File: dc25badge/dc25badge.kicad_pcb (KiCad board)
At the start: 2 copper layers, 150.7 x 59.7 mm, 110 parts, among them P1 BATT, P2 USB_OTG, P3 CONN_CORTEX, SW1 RESET, SW2 PWR, SW3 MODE, SW4 BRIGHT, U1 MIC5305, U10 APA102, U11 APA102, U12 APA102, U13 APA102, U14 APA102, U15 APA102, U16 APA102, U17 APA102, U18 APA102, U19 APA102, U2 TPS61232, U20 APA102, U21 APA102, U22 APA102, U23 APA102, U24 APA102, U25 APA102, U26 APA102, U27 APA102, U28 APA102, U29 APA102, U3 ATSAMD21E18A-AU, U30 APA102, U31 APA102, U32 APA102, U33 APA102, U34 APA102, U35 APA102, U36 APA102, U37 APA102, U38 APA102, U39 APA102, U4 74AHCT125, U40 APA102, U41 APA102, U42 APA102, U43 APA102, U44 APA102, U45 APA102, U46 APA102, U47 APA102, U48 APA102, U49 APA102, U5 APA102, U50 APA102, U51 APA102, U52 APA102, U53 APA102, U54 APA102, U55 APA102, U56 APA102, U57 APA102, U58 APA102, U59 APA102, U6 APA102, U60 APA102, U61 APA102, U62 APA102, U63 APA102, U64 APA102, U7 APA102, U8 APA102, U9 APA102, Y1 32.768k

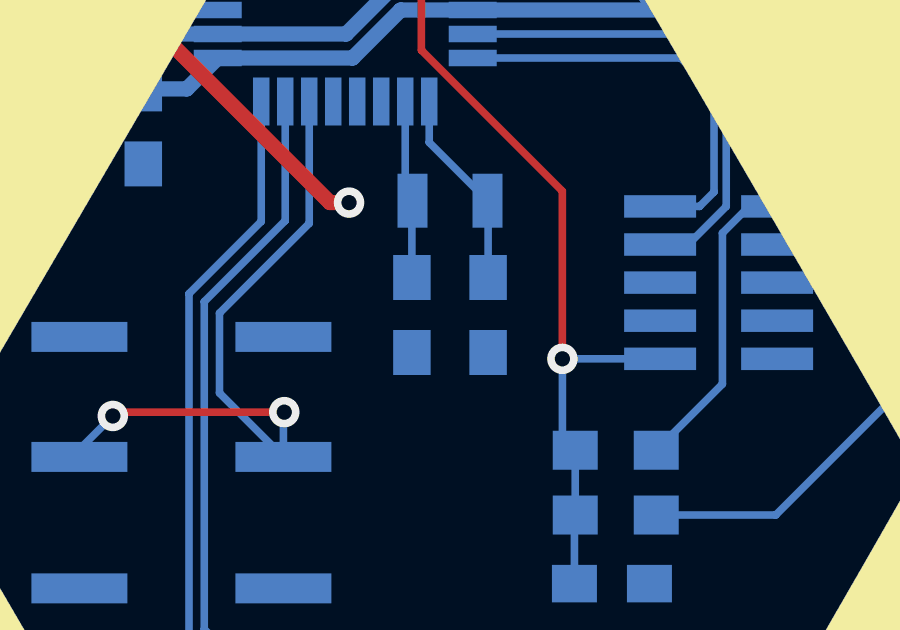
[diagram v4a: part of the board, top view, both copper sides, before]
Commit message: Switch to 0603 caps on oscillator.
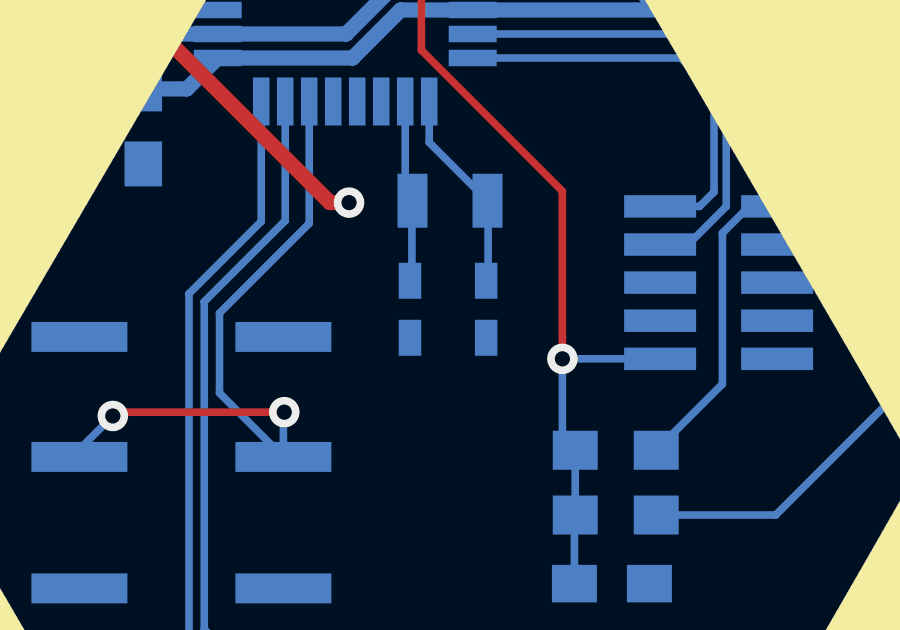
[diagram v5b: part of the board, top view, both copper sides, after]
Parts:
- C12, C13: footprint Capacitors_SMD:C_0805_HandSoldering -> Capacitors_SMD:C_0603_HandSoldering
- L1: value L_Core_Ferrite -> 1uH
- moved C12 0.20 mm to (76.3, 51.1)
- moved C13 0.20 mm to (78.9, 51.1)
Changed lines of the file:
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@@
   )
   (setup
-    (last_trace_width 1.016)
+    (last_trace_width 0.1524)
     (user_trace_width 0.1524)
     (user_trace_width 0.254)
@@
   )
   (module Capacitors_SMD:C_0805_HandSoldering (layer B.Cu)
-    (at 76.3905 51.2445 270)
-    (descr "Capacitor SMD 0805, hand soldering")
-    (tags "capacitor 0805")
-    (attr smd)
-    (fp_text reference C12 (at -1.778 1.397 270) (layer B.SilkS)
-      (effects (font (size 0.4 0.4) (thickness 0.1)) (justify mirror))
-    )
-    (fp_text value 22pF (at 0 -2.1 270) (layer B.Fab) hide
-      (effects (font (size 1 1) (thickness 0.15)) (justify mirror))
-    )
-    (fp_line (start -1 -0.625) (end -1 0.625) (layer B.Fab) (width 0.15))
-    (fp_line (start 1 -0.625) (end -1 -0.625) (layer B.Fab) (width 0.15))
-    (fp_line (start 1 0.625) (end 1 -0.625) (layer B.Fab) (width 0.15))
-    (fp_line (start -1 0.625) (end 1 0.625) (layer B.Fab) (width 0.15))
-    (fp_line (start -2.3 1) (end 2.3 1) (layer B.CrtYd) (width 0.05))
-    (fp_line (start -2.3 -1) (end 2.3 -1) (layer B.CrtYd) (width 0.05))
-    (fp_line (start -2.3 1) (end -2.3 -1) (layer B.CrtYd) (width 0.05))
-    (fp_line (start 2.3 1) (end 2.3 -1) (layer B.CrtYd) (width 0.05))
-    (fp_line (start 0.5 0.85) (end -0.5 0.85) (layer B.SilkS) (width 0.15))
-    (fp_line (start -0.5 -0.85) (end 0.5 -0.85) (layer B.SilkS) (width 0.15))
-    (pad 1 smd rect (at -1.25 0 270) (size 1.5 1.25) (layers B.Cu B.Paste B.Mask)
-      (net 7 XOUT32))
-    (pad 2 smd rect (at 1.25 0 270) (size 1.5 1.25) (layers B.Cu B.Paste B.Mask)
-      (net 1 GND))
-    (model Capacitors_SMD.3dshapes/C_0805_HandSoldering.wrl
-      (at (xyz 0 0 0))
-      (scale (xyz 1 1 1))
-      (rotate (xyz 0 0 0))
-    )
-  )
-  (module Capacitors_SMD:C_0805_HandSoldering (layer B.Cu)
-    (at 78.9305 51.2445 270)
-    (descr "Capacitor SMD 0805, hand soldering")
-    (tags "capacitor 0805")
-    (attr smd)
-    (fp_text reference C13 (at -1.651 -1.397 270) (layer B.SilkS)
-      (effects (font (size 0.4 0.4) (thickness 0.1)) (justify mirror))
-    )
-    (fp_text value 22pF (at 0 -2.1 270) (layer B.Fab) hide
-      (effects (font (size 1 1) (thickness 0.15)) (justify mirror))
-    )
-    (fp_line (start -1 -0.625) (end -1 0.625) (layer B.Fab) (width 0.15))
-    (fp_line (start 1 -0.625) (end -1 -0.625) (layer B.Fab) (width 0.15))
-    (fp_line (start 1 0.625) (end 1 -0.625) (layer B.Fab) (width 0.15))
-    (fp_line (start -1 0.625) (end 1 0.625) (layer B.Fab) (width 0.15))
-    (fp_line (start -2.3 1) (end 2.3 1) (layer B.CrtYd) (width 0.05))
-    (fp_line (start -2.3 -1) (end 2.3 -1) (layer B.CrtYd) (width 0.05))
-    (fp_line (start -2.3 1) (end -2.3 -1) (layer B.CrtYd) (width 0.05))
-    (fp_line (start 2.3 1) (end 2.3 -1) (layer B.CrtYd) (width 0.05))
-    (fp_line (start 0.5 0.85) (end -0.5 0.85) (layer B.SilkS) (width 0.15))
-    (fp_line (start -0.5 -0.85) (end 0.5 -0.85) (layer B.SilkS) (width 0.15))
-    (pad 1 smd rect (at -1.25 0 270) (size 1.5 1.25) (layers B.Cu B.Paste B.Mask)
-      (net 8 XIN32))
-    (pad 2 smd rect (at 1.25 0 270) (size 1.5 1.25) (layers B.Cu B.Paste B.Mask)
-      (net 1 GND))
-    (model Capacitors_SMD.3dshapes/C_0805_HandSoldering.wrl
-      (at (xyz 0 0 0))
-      (scale (xyz 1 1 1))
-      (rotate (xyz 0 0 0))
-    )
-  )
-  (module Capacitors_SMD:C_0805_HandSoldering (layer B.Cu)
     (at 101.219 67.818 270)
     (descr "Capacitor SMD 0805, hand soldering")
@@
       (effects (font (size 0.5 0.5) (thickness 0.1)) (justify mirror))
     )
-    (fp_text value L_Core_Ferrite (at 0 -3.4 180) (layer B.Fab) hide
+    (fp_text value 1uH (at 0 -3.4 180) (layer B.Fab) hide
       (effects (font (size 1 1) (thickness 0.15)) (justify mirror))
     )
@@
     )
   )
+  (module Capacitors_SMD:C_0603_HandSoldering (layer B.Cu)
+    (at 76.327 51.054 270)
+    (descr "Capacitor SMD 0603, hand soldering")
+    (tags "capacitor 0603")
+    (attr smd)
+    (fp_text reference C12 (at -1.27 1.143 270) (layer B.SilkS)
+      (effects (font (size 0.4 0.4) (thickness 0.1)) (justify mirror))
+    )
+    (fp_text value 22pF (at 0 -1.9 270) (layer B.Fab) hide
+      (effects (font (size 1 1) (thickness 0.15)) (justify mirror))
+    )
+    (fp_line (start -0.8 -0.4) (end -0.8 0.4) (layer B.Fab) (width 0.15))
+    (fp_line (start 0.8 -0.4) (end -0.8 -0.4) (layer B.Fab) (width 0.15))
+    (fp_line (start 0.8 0.4) (end 0.8 -0.4) (layer B.Fab) (width 0.15))
+    (fp_line (start -0.8 0.4) (end 0.8 0.4) (layer B.Fab) (width 0.15))
+    (fp_line (start -1.85 0.75) (end 1.85 0.75) (layer B.CrtYd) (width 0.05))
+    (fp_line (start -1.85 -0.75) (end 1.85 -0.75) (layer B.CrtYd) (width 0.05))
+    (fp_line (start -1.85 0.75) (end -1.85 -0.75) (layer B.CrtYd) (width 0.05))
+    (fp_line (start 1.85 0.75) (end 1.85 -0.75) (layer B.CrtYd) (width 0.05))
+    (fp_line (start -0.35 0.6) (end 0.35 0.6) (layer B.SilkS) (width 0.15))
+    (fp_line (start 0.35 -0.6) (end -0.35 -0.6) (layer B.SilkS) (width 0.15))
+    (pad 1 smd rect (at -0.95 0 270) (size 1.2 0.75) (layers B.Cu B.Paste B.Mask)
+      (net 7 XOUT32))
+    (pad 2 smd rect (at 0.95 0 270) (size 1.2 0.75) (layers B.Cu B.Paste B.Mask)
+      (net 1 GND))
+    (model Capacitors_SMD.3dshapes/C_0603_HandSoldering.wrl
+      (at (xyz 0 0 0))
+      (scale (xyz 1 1 1))
+      (rotate (xyz 0 0 0))
+    )
+  )
+  (module Capacitors_SMD:C_0603_HandSoldering (layer B.Cu)
+    (at 78.867 51.054 270)
+    (descr "Capacitor SMD 0603, hand soldering")
+    (tags "capacitor 0603")
+    (attr smd)
+    (fp_text reference C13 (at -1.27 -1.143 270) (layer B.SilkS)
+      (effects (font (size 0.4 0.4) (thickness 0.1)) (justify mirror))
+    )
+    (fp_text value 22pF (at 0 -1.9 270) (layer B.Fab) hide
+      (effects (font (size 1 1) (thickness 0.15)) (justify mirror))
+    )
+    (fp_line (start -0.8 -0.4) (end -0.8 0.4) (layer B.Fab) (width 0.15))
+    (fp_line (start 0.8 -0.4) (end -0.8 -0.4) (layer B.Fab) (width 0.15))
+    (fp_line (start 0.8 0.4) (end 0.8 -0.4) (layer B.Fab) (width 0.15))
+    (fp_line (start -0.8 0.4) (end 0.8 0.4) (layer B.Fab) (width 0.15))
+    (fp_line (start -1.85 0.75) (end 1.85 0.75) (layer B.CrtYd) (width 0.05))
+    (fp_line (start -1.85 -0.75) (end 1.85 -0.75) (layer B.CrtYd) (width 0.05))
+    (fp_line (start -1.85 0.75) (end -1.85 -0.75) (layer B.CrtYd) (width 0.05))
+    (fp_line (start 1.85 0.75) (end 1.85 -0.75) (layer B.CrtYd) (width 0.05))
+    (fp_line (start -0.35 0.6) (end 0.35 0.6) (layer B.SilkS) (width 0.15))
+    (fp_line (start 0.35 -0.6) (end -0.35 -0.6) (layer B.SilkS) (width 0.15))
+    (pad 1 smd rect (at -0.95 0 270) (size 1.2 0.75) (layers B.Cu B.Paste B.Mask)
+      (net 8 XIN32))
+    (pad 2 smd rect (at 0.95 0 270) (size 1.2 0.75) (layers B.Cu B.Paste B.Mask)
+      (net 1 GND))
+    (model Capacitors_SMD.3dshapes/C_0603_HandSoldering.wrl
+      (at (xyz 0 0 0))
+      (scale (xyz 1 1 1))
+      (rotate (xyz 0 0 0))
+    )
+  )
   (gr_line (start 26.67 86.868) (end 44.323 56.515) (angle 90) (layer Edge.Cuts) (width 0.15))
   (gr_line (start 158.496 86.868) (end 26.67 86.868) (angle 90) (layer Edge.Cuts) (width 0.15))
@@
   (gr_line (start 44.323 56.515) (end 27.305 27.178) (angle 90) (layer Edge.Cuts) (width 0.15))
   (via (at 143.891 49.276) (size 1.016) (drill 0.508) (layers F.Cu B.Cu) (net 0))
-  (segment (start 123.079 43.453) (end 121.558 43.453) (width 1.016) (layer B.Cu) (net 1) (status 400000))
-  (segment (start 124.333 35.433) (end 124.333 33.909) (width 1.016) (layer B.Cu) (net 1) (status 800000))
+  (segment (start 123.079 43.453) (end 121.558 43.453) (width 1.016) (layer B.Cu) (net 1))
+  (segment (start 124.333 35.433) (end 124.333 33.909) (width 1.016) (layer B.Cu) (net 1))
   (segment (start 121.539 38.227) (end 124.333 35.433) (width 1.016) (layer B.Cu) (net 1))
   (via (at 121.539 38.227) (size 1.016) (drill 0.508) (layers F.Cu B.Cu) (net 1))
@@
   (segment (start 149.175 82.15) (end 151.825 82.15) (width 0.254) (layer F.Cu) (net 151))
   (segment (start 149.175 84) (end 151.825 84) (width 0.254) (layer F.Cu) (net 152))
-  (segment (start 125.079 43.453) (end 125.079 40.021) (width 1.016) (layer B.Cu) (net 157) (status 400000))
+  (segment (start 125.079 43.453) (end 125.079 40.021) (width 1.016) (layer B.Cu) (net 157))
   (segment (start 125.079 40.021) (end 127.235 40.021) (width 1.016) (layer B.Cu) (net 157))
   (segment (start 127.235 40.021) (end 105.954 40.021) (width 0.762) (layer B.Cu) (net 157))

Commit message: Fixup trace clearances.
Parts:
- P3: value CONN_CORTEX -> CORTEX
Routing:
- net +5V: track 257.1 -> 261.4 mm, vias 31 -> 33
- net GND: track 254.6 -> 258.0 mm
- net /VBAT: track 91.1 -> 89.0 mm
- net Net-(U22-Pad6): track 7.73 -> 7.18 mm
- net Net-(U24-Pad1): track 7.73 -> 7.20 mm
- net (no net): vias 1 -> 0

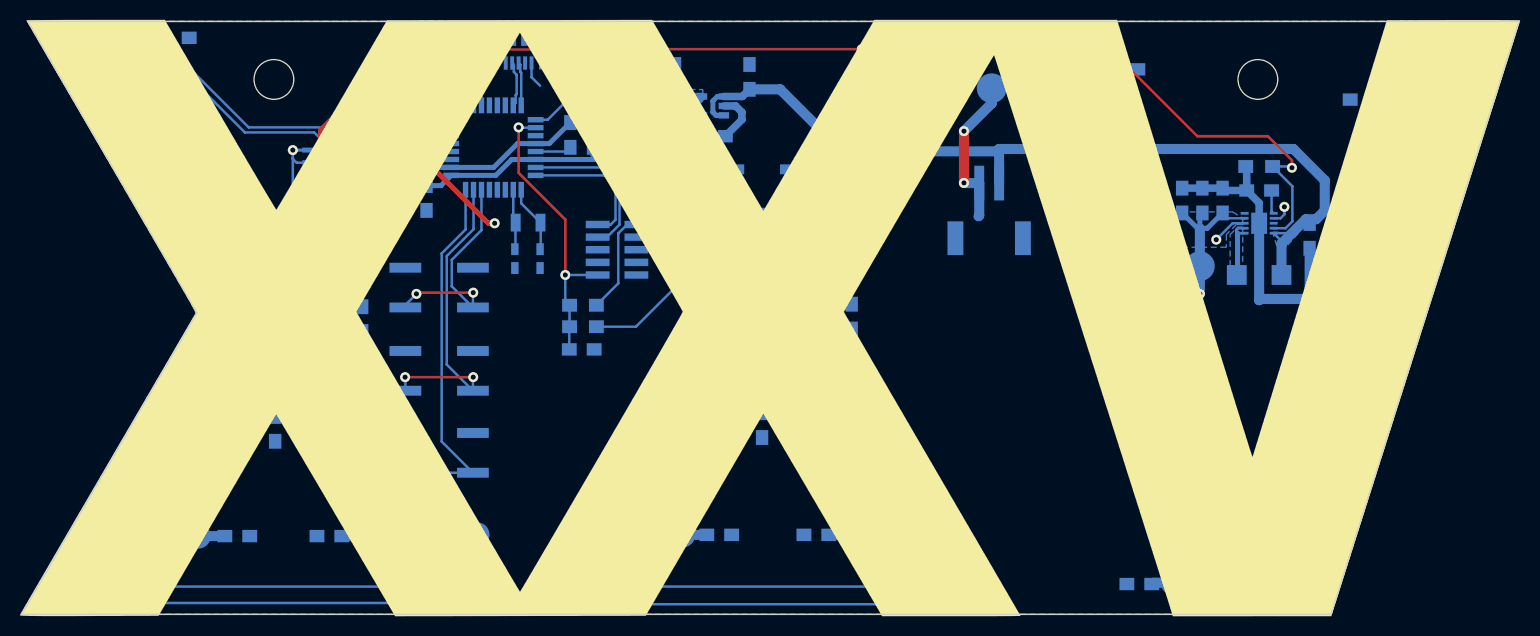
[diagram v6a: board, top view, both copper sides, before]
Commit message: Move to 8mil mins.
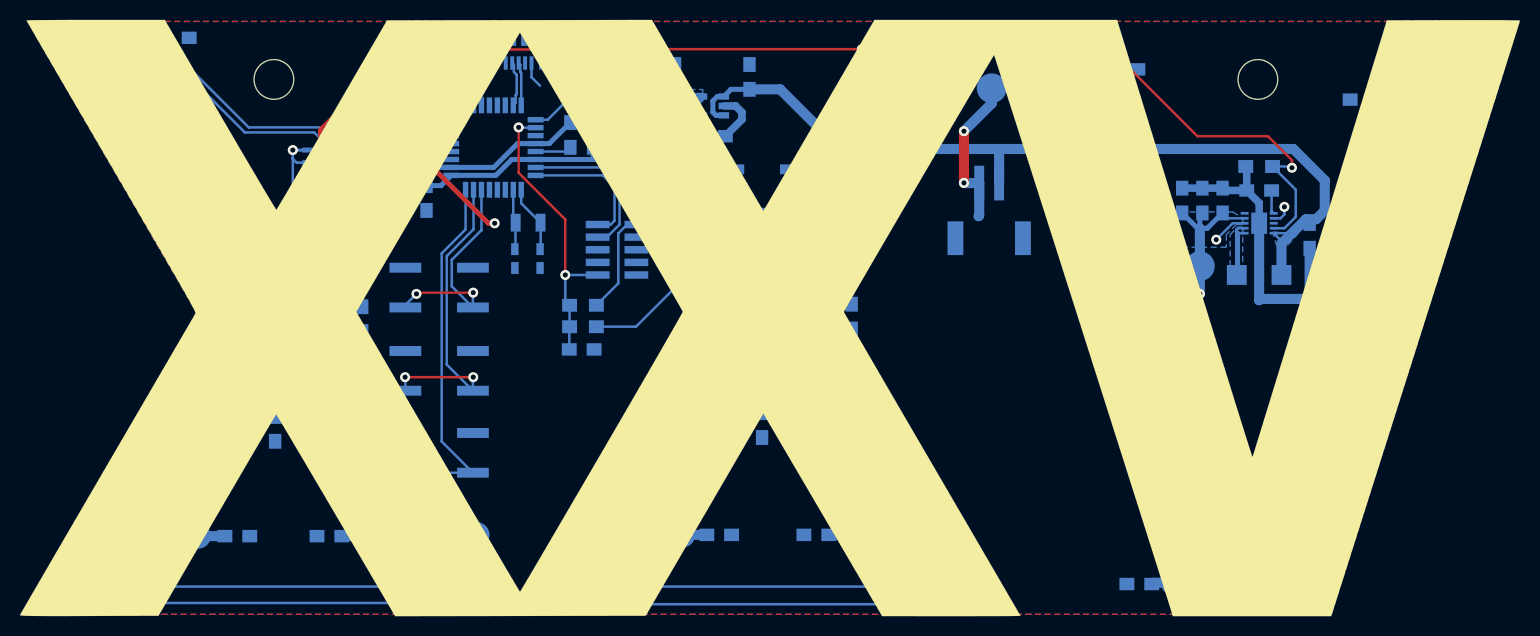
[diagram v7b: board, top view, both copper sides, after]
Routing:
- net Net-(U23-Pad2): track 7.99 -> 8.97 mm
- net Net-(U44-Pad5): track 9.06 -> 8.34 mm
- net Net-(U14-Pad1): track 7.51 -> 6.86 mm
- net Net-(U54-Pad2): track 7.96 -> 8.57 mm
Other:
- board outline removed
- net class Current: clearance 0.1524 -> 0.2032; trace_width 0.508 -> 0.254
- net class Default: clearance 0.1524 -> 0.2032; trace_width 0.1524 -> 0.254
- net class USB added: clearance 0.1524, trace_width 0.2032, via_dia 1.016, via_drill 0.508
- rule trace_clearance: 0.1524 -> 0.2032
- rule trace_min: 0.1524 -> 0.2032

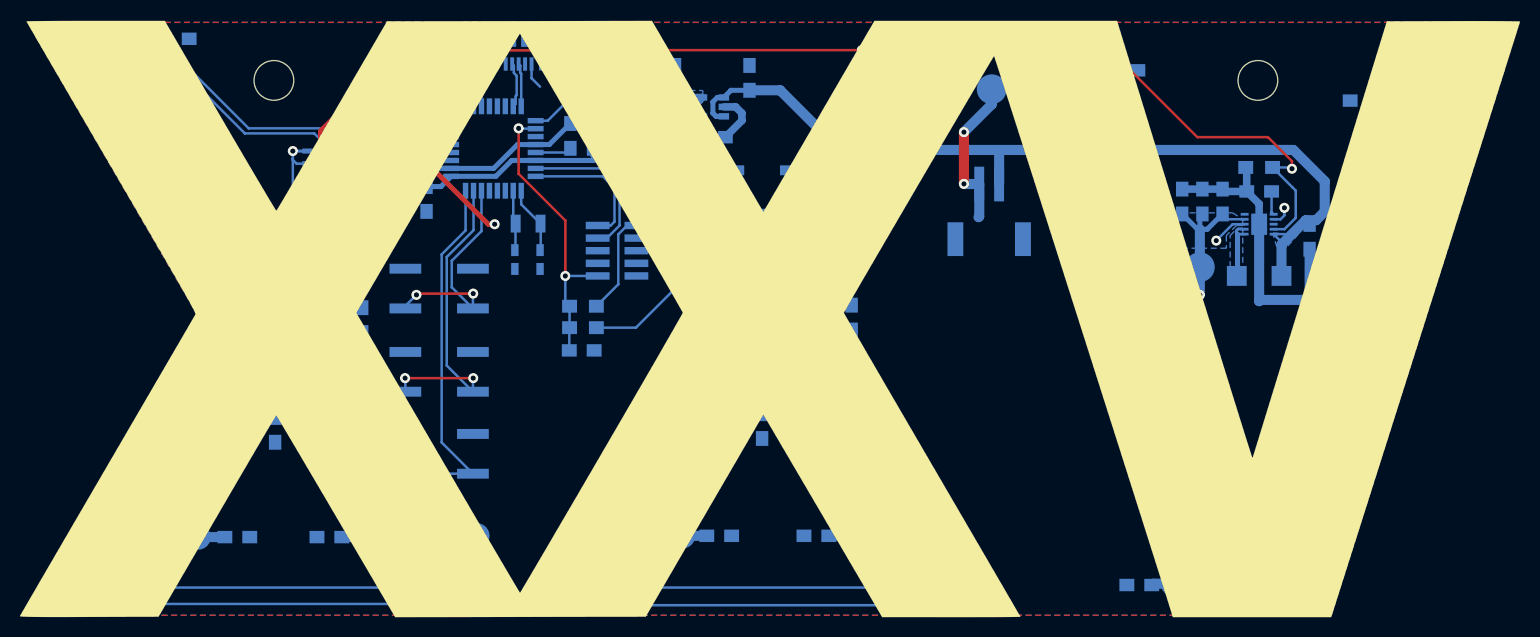
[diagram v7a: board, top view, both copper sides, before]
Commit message: Readd cuts.
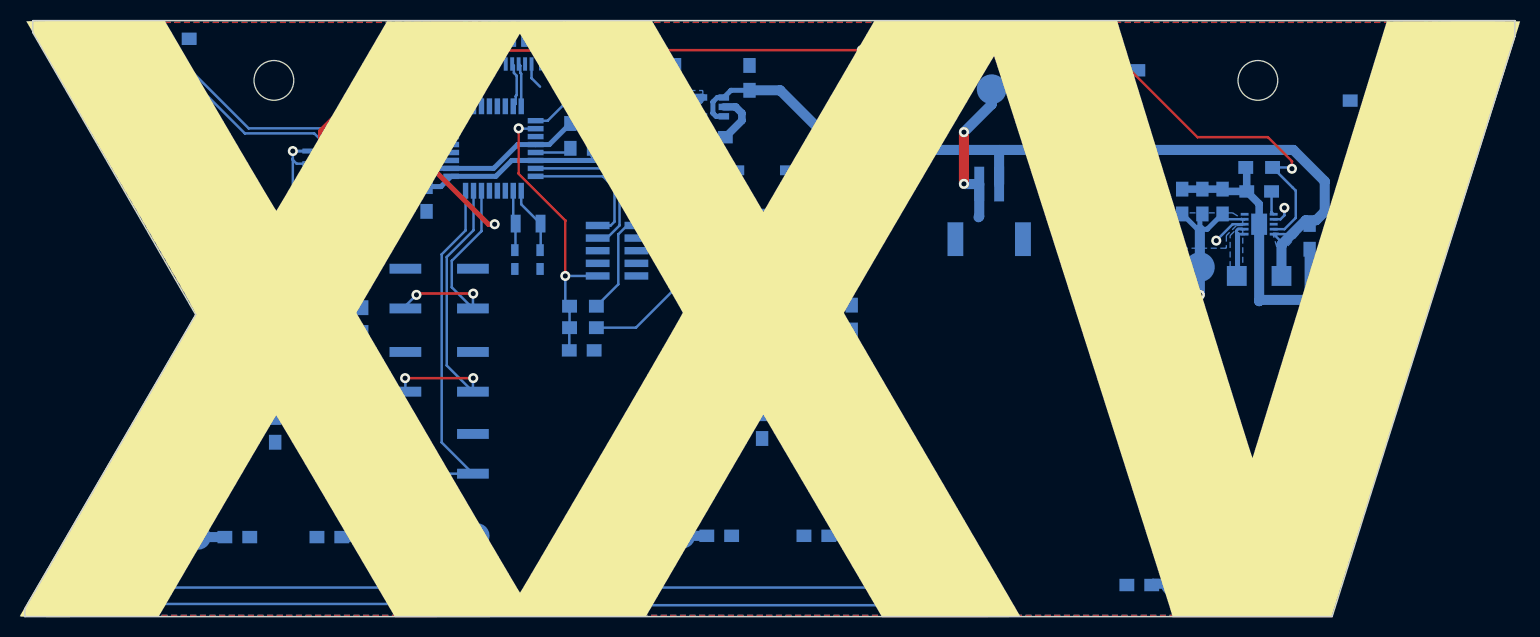
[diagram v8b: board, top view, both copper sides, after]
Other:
- board outline added: 150 x 60 mm
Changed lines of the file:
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@@
     (links 358)
     (no_connects 0)
-    (area 26.344399 24.9826 177.683228 89.1374)
+    (area 26.293599 24.9318 177.734028 89.1882)
     (thickness 1.6)
-    (drawings 0)
+    (drawings 8)
     (tracks 1297)
     (zones 0)
@@
     (35 F.Paste user)
     (36 B.SilkS user)
-    (37 F.SilkS user hide)
+    (37 F.SilkS user)
     (38 B.Mask user)
     (39 F.Mask user)
@@
     )
   )
+  (gr_line (start 177 28.6) (end 177 27) (angle 90) (layer Edge.Cuts) (width 0.15))
+  (gr_line (start 158.6 87) (end 177 28.6) (angle 90) (layer Edge.Cuts) (width 0.15))
+  (gr_line (start 27 87) (end 158.6 87) (angle 90) (layer Edge.Cuts) (width 0.15))
+  (gr_line (start 27 86.2) (end 27 87) (angle 90) (layer Edge.Cuts) (width 0.15))
+  (gr_line (start 44.2 56.6) (end 27 86.2) (angle 90) (layer Edge.Cuts) (width 0.15))
+  (gr_line (start 27.8 28.2) (end 44.2 56.6) (angle 90) (layer Edge.Cuts) (width 0.15))
+  (gr_line (start 27.8 27) (end 27.8 28.2) (angle 90) (layer Edge.Cuts) (width 0.15))
+  (gr_line (start 177 27) (end 27.8 27) (angle 90) (layer Edge.Cuts) (width 0.15))
   (segment (start 123.079 43.453) (end 123.079 46.72) (width 1.016) (layer B.Cu) (net 1))
   (segment (start 123.079 46.72) (end 122.9995 46.7995) (width 1.016) (layer B.Cu) (net 1))
@@
   (segment (start 67.825 84) (end 68.3492 84) (width 0.254) (layer F.Cu) (net 136))
   (segment (start 68.675 78) (end 68.431 78) (width 0.254) (layer F.Cu) (net 136))
-  (segment (start 117.175 79.85) (end 117.175 80.2688) (width 0.254) (layer F.Cu) (net 137) (status 400000))
-  (segment (start 118.0846 84.0904) (end 116.325 85.85) (width 0.254) (layer F.Cu) (net 137) (status 800000))
+  (segment (start 117.175 79.85) (end 117.175 80.2688) (width 0.254) (layer F.Cu) (net 137))
+  (segment (start 118.0846 84.0904) (end 116.325 85.85) (width 0.254) (layer F.Cu) (net 137))
   (segment (start 118.0846 81.1784) (end 118.0846 84.0904) (width 0.254) (layer F.Cu) (net 137))
   (segment (start 117.175 80.2688) (end 118.0846 81.1784) (width 0.254) (layer F.Cu) (net 137))
-  (segment (start 117.175 78) (end 117.072 78) (width 0.254) (layer F.Cu) (net 138) (status C00000))
-  (segment (start 117.072 78) (end 115.8494 79.2226) (width 0.254) (layer F.Cu) (net 138) (status 400000))
-  (segment (start 117.602 82.723) (end 116.325 84) (width 0.254) (layer F.Cu) (net 138) (status 800000))
+  (segment (start 117.175 78) (end 117.072 78) (width 0.254) (layer F.Cu) (net 138))
+  (segment (start 117.072 78) (end 115.8494 79.2226) (width 0.254) (layer F.Cu) (net 138))
+  (segment (start 117.602 82.723) (end 116.325 84) (width 0.254) (layer F.Cu) (net 138))
   (segment (start 117.602 81.407) (end 117.602 82.723) (width 0.254) (layer F.Cu) (net 138))
   (segment (start 117.1956 81.0006) (end 117.602 81.407) (width 0.254) (layer F.Cu) (net 138))
